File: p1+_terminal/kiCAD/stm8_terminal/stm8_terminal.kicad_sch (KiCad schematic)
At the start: 24 parts, among them J1 USB_A, J2 PS/2 Female, J3 TV out, SW1 SW_SPST, SW2 local echo, SW3 baud rate 1, SW4 baud rate 0, T1 step down transformer, U1 LD1117V50-TO-220, Y1 24 Mhz

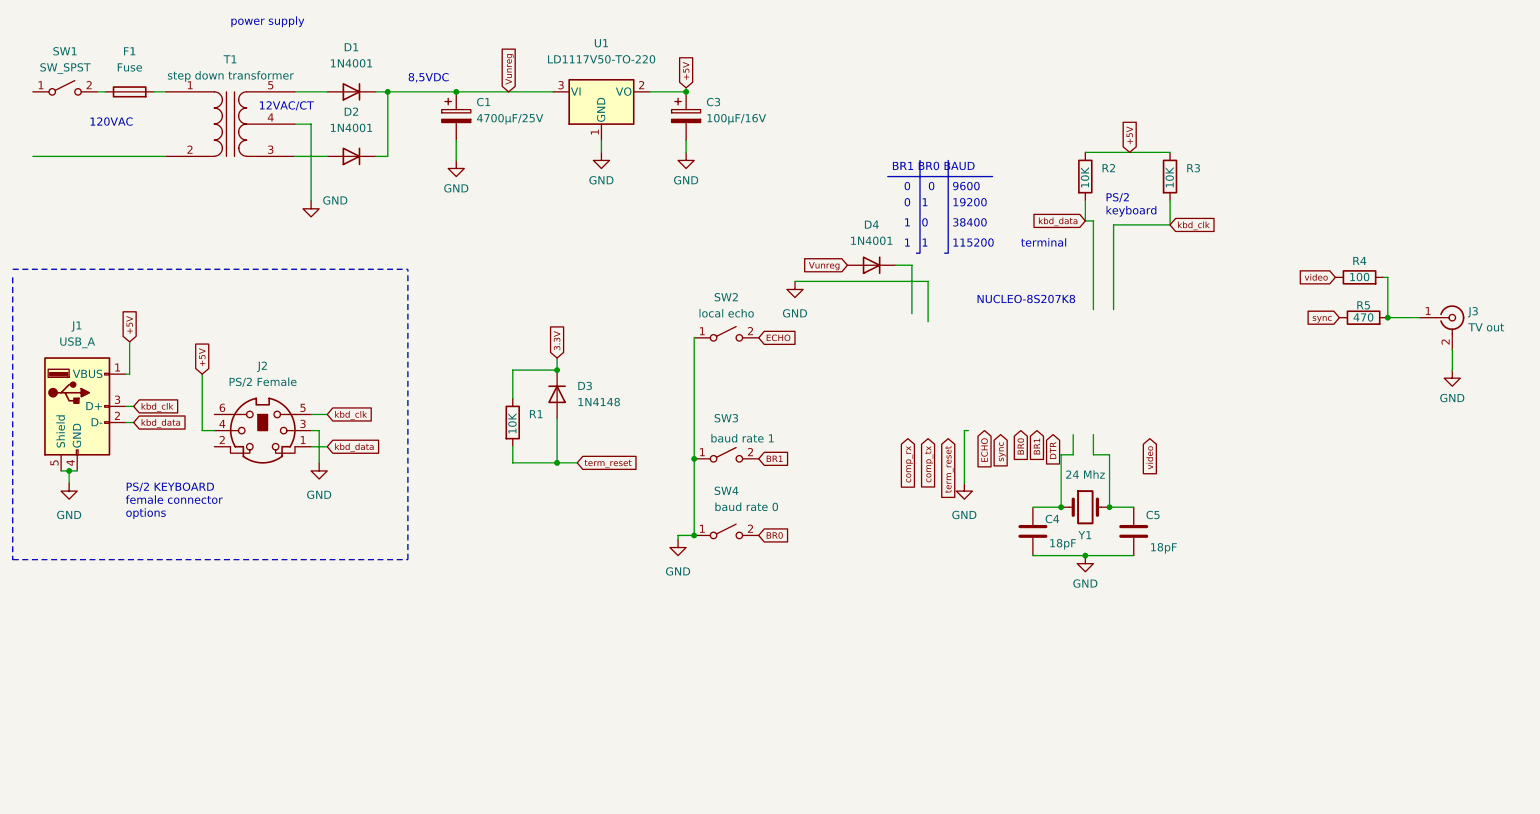
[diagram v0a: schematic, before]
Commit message: Ajout du sous-projet p1+_drive
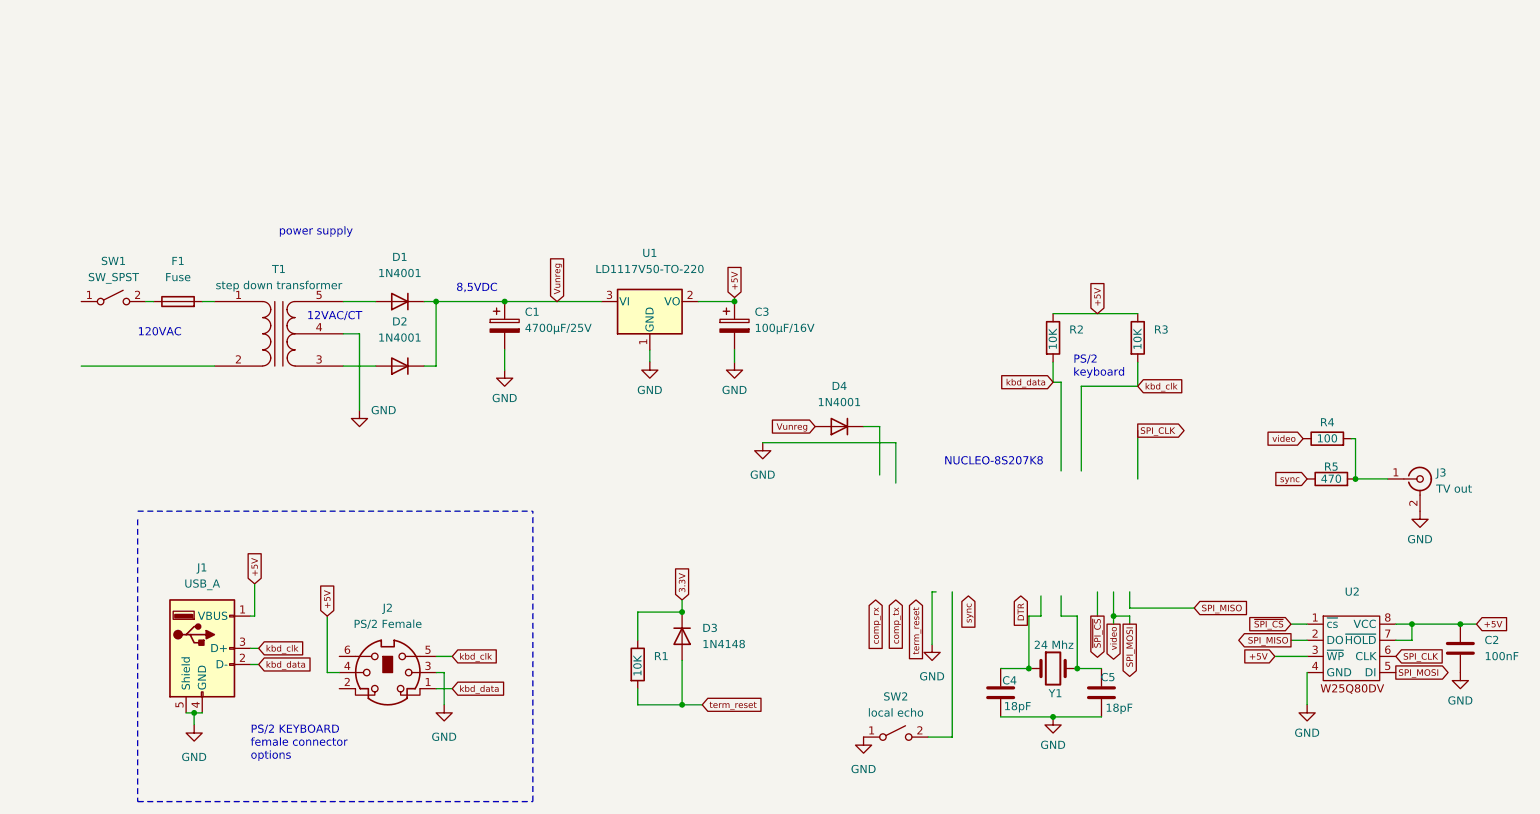
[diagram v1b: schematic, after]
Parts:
- removed SW3: baud rate 1, symbol Switch:SW_SPST
- removed SW4: baud rate 0, symbol Switch:SW_SPST
- added C2: 100nF, symbol Device:C
- added U2: ~, symbol project_lib:W25Q80DV
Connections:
- net +5V: now also C2.1, U2.3 (~{WP}), U2.7 (~{HOLD}), U2.8 (VCC)
- net GND: now also C2.2, U2.4 (GND)
- net ECHO: no longer names the net of SW2.2 (B)
- net video renamed SPI_MOSI
- net SPI_MOSI: now also U2.5 (DI)
- new net SPI_CLK: U2.6 (CLK)
- new net SPI_MISO: U2.2 (DO)
- new net ~{SPI_CS}: U2.1 (~{cs})
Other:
- note removed: "0"
- note removed: "0 1"
- note removed: "1 0"
- note removed: "1 1"
- note removed: "115200"
- note removed: "19200"
- note removed: "38400"
- note removed: "9600"
- note removed: "BR1 BR0 BAUD"
- note removed: "terminal"
- moved on the sheet: C1, C3, C4, C5, D1, D2, D3, D4, F1, J1, J2, J3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
